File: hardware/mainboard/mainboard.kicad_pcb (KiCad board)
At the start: 2 copper layers, 12 parts, among them J1 Conn_01x03, J2 Conn_01x03, J3 Conn_01x03, J4 Conn_01x03, J5 Conn_01x03, SW1 Rotary_Encoder_Switch

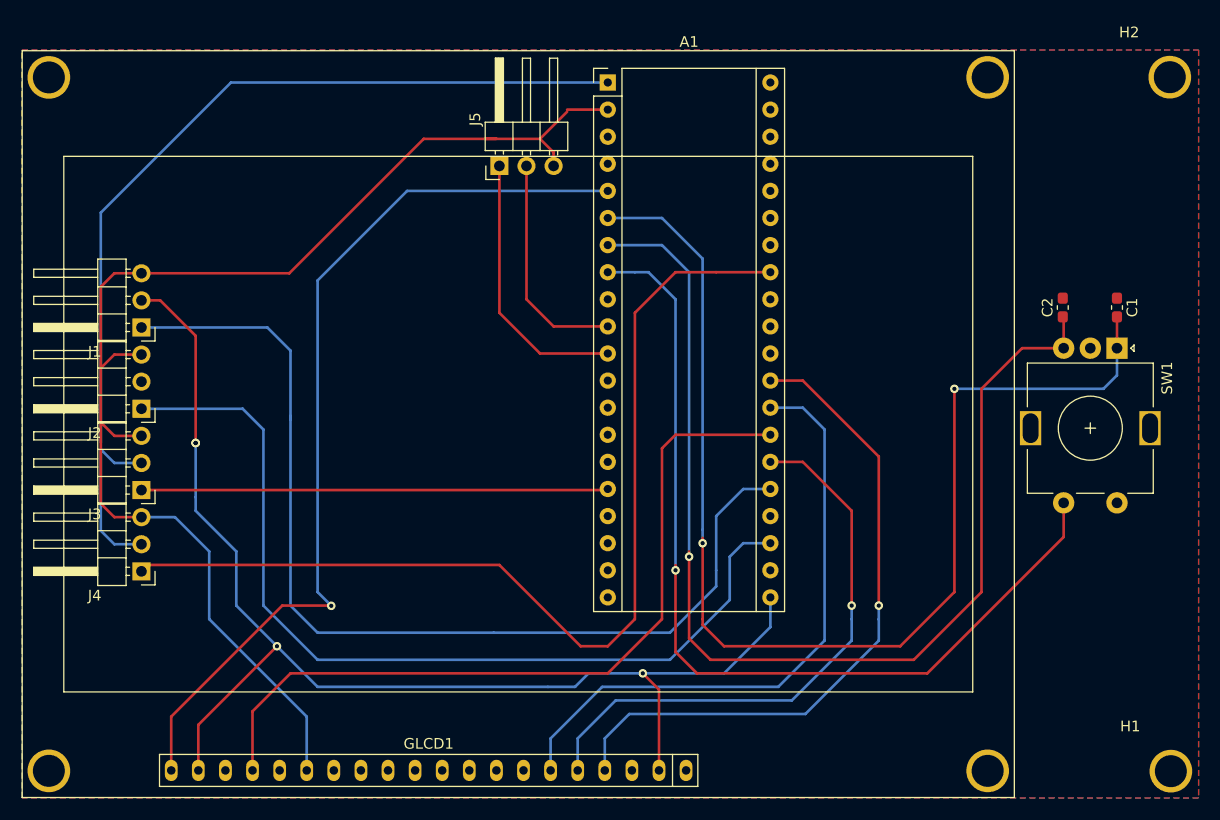
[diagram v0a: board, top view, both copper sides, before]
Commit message: generated gerber files for jlcpcb
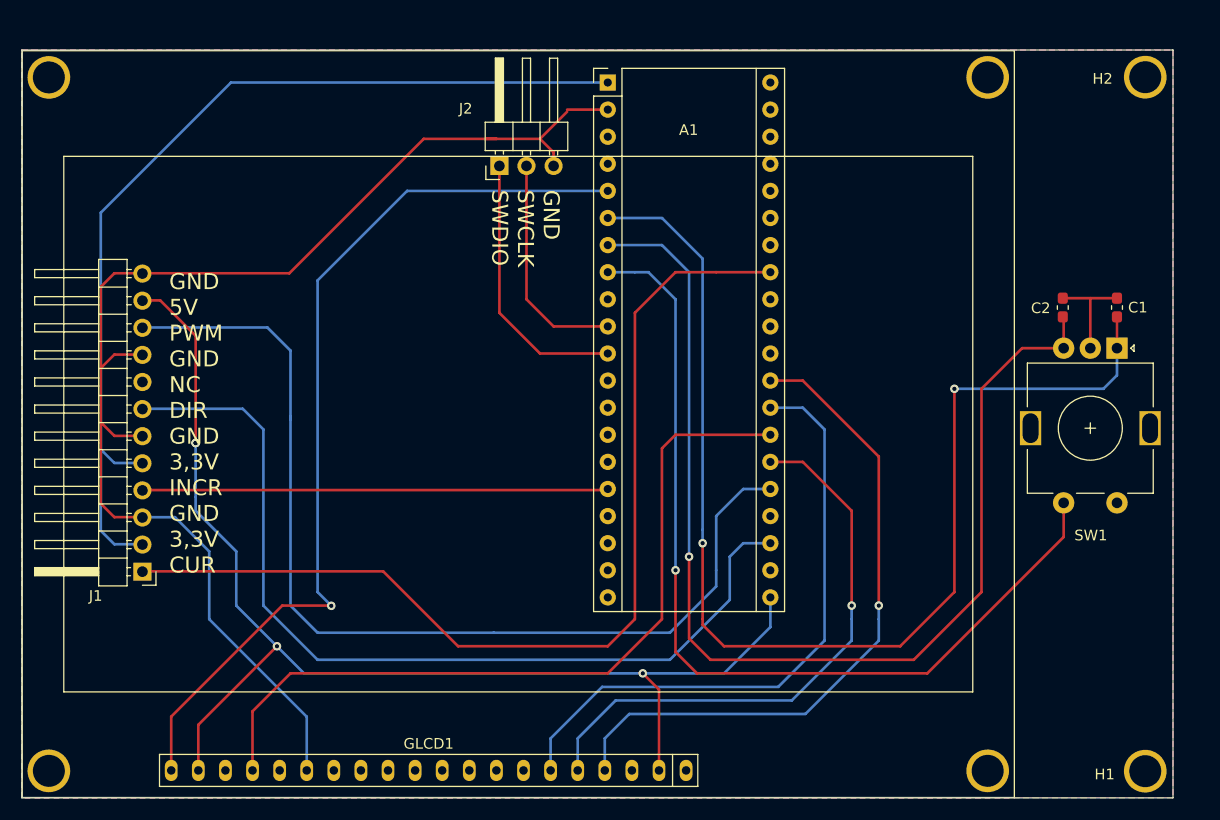
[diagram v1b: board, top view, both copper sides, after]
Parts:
- removed J3, J4, J5: Conn_01x03, Connector_PinHeader_2.54mm:PinHeader_1x03_P2.54mm_Horizontal
- added REF**: OSHW-Logo2_14.6x12mm_SilkScreen, Symbol:OSHW-Logo2_14.6x12mm_SilkScreen, B.Cu at (98.9, 90.0)
- J1: value Conn_01x03 -> Conn_01x12_MountingPin; footprint Connector_PinHeader_2.54mm:PinHeader_1x03_P2.54mm_Horizontal -> Connector_PinHeader_2.54mm:PinHeader_1x12_P2.54mm_Horizontal
- moved J2 40.5 mm to (100.9, 65.5), turned to 90 degrees
- moved J1 22.9 mm to (67.4, 103.5)
- moved H1 2.40 mm to (157.6, 122.2)
- moved H2 2.30 mm to (157.6, 57.1)
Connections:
- J1 pad 1: ESC_PWM -> CUR_ADC
- J1 pad 2: +5V -> +3V3
- J2 pad 1: ESC_DIR -> SWDIO
- J2 pad 2: Net-(J2-Pad2) -> SWCLK
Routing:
- net GND: track 123.7 -> 133.5 mm
- net +5V: track 116.6 -> 115.9 mm
- net +3V3: track 90.5 -> 91.1 mm
- net RTE_CW: track 105.7 -> 105.2 mm
- net RTE_CCW: track 112.1 -> 111.6 mm
- net RTE_BTN: track 86.7 -> 86.2 mm
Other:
- board outline added: 107.9 x 70.1 mm
- copper layers 2 -> 4
- net class Default: clearance 0.2 -> 0.127; trace_width 0.25 -> 0.127; via_dia 0.8 -> 0.6; via_drill 0.4 -> 0.3
- rule pad_to_mask_clearance: 0.05 -> 0
- rule trace_clearance: 0.2 -> 0.127
- rule trace_min: 0.2 -> 0.127
- rule via_min_size: 0.4 -> 0.6
- board text added: "Drill-Ctrl v0.1"
- board text added: "GND 5V PWM GND NC DIR GND 3,3V INCR GND 3,3V CUR"
- board text added: "GND SWCLK SWDIO"
